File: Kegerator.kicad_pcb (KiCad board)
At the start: 2 copper layers, 200 x 21 mm, 17 parts, among them J1 Buttons, J2 LCD, J3 Temperature, J4 Programmer, J5 Control, U1 ESP32-S2-WROVER, U2 MCP1700

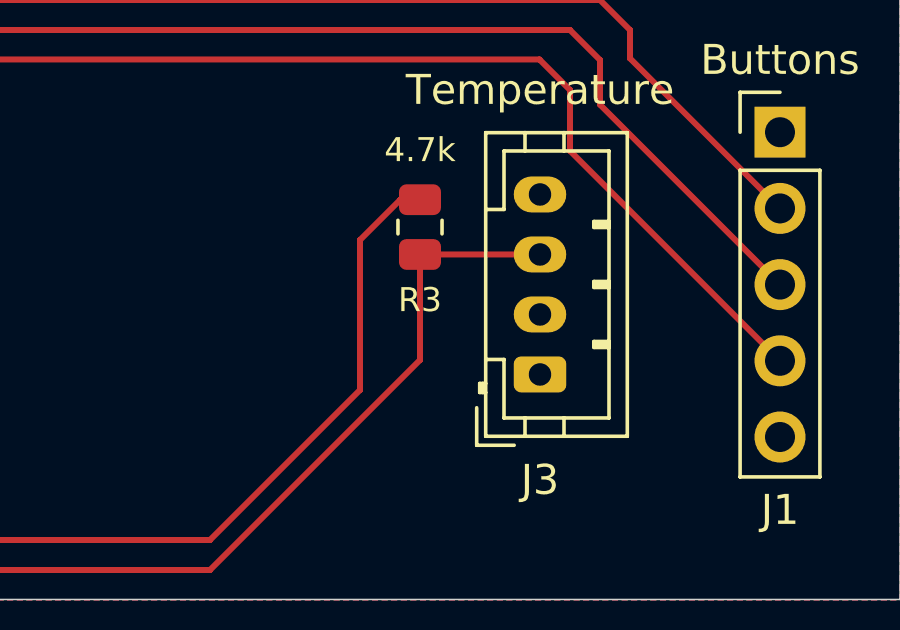
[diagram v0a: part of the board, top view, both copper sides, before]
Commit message: Allowing the temperature sensor to be able to be both really powered or parasitic power
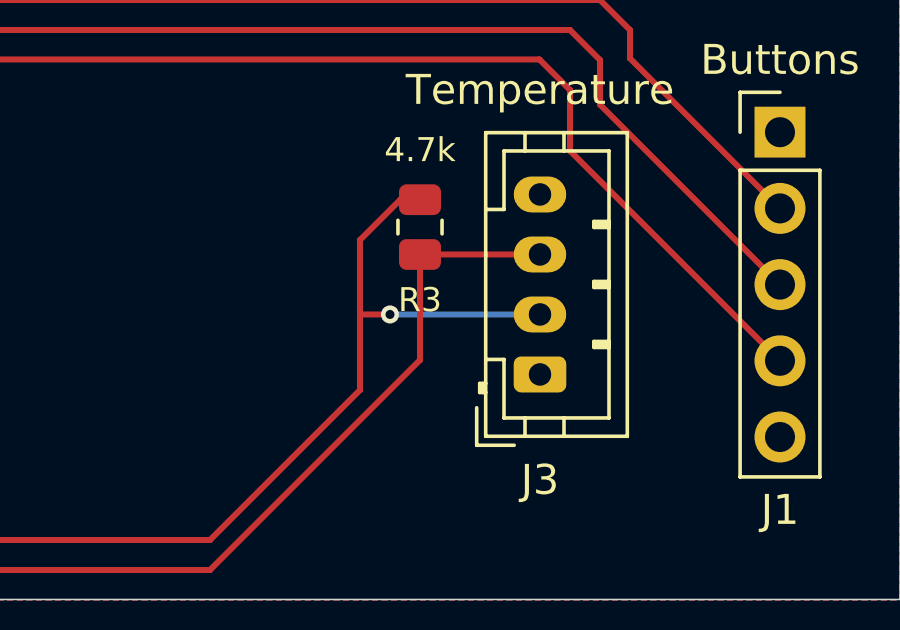
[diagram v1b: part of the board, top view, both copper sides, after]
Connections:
- J3 pad 2: unconnected-(J3-Pin_2-Pad2) -> +3V3
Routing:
- net +3V3: track 219.8 -> 225.8 mm, vias 2 -> 3
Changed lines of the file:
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@@
 	(net 37 "unconnected-(U1-IO08-Pad11)")
 	(net 38 "unconnected-(U1-IO37-Pad31)")
-	(net 39 "unconnected-(J3-Pin_2-Pad2)")
-	(net 40 "unconnected-(J3-Pin_1-Pad1)")
-	(net 41 "BOOT")
-	(net 42 "unconnected-(U1-IO14-Pad17)")
-	(net 43 "/HEAT")
-	(net 44 "HEATER")
-	(net 45 "/COOL")
-	(net 46 "unconnected-(J1-Pin_1-Pad1)")
+	(net 39 "unconnected-(J3-Pin_1-Pad1)")
+	(net 40 "BOOT")
+	(net 41 "unconnected-(U1-IO14-Pad17)")
+	(net 42 "/HEAT")
+	(net 43 "HEATER")
+	(net 44 "/COOL")
+	(net 45 "unconnected-(J1-Pin_1-Pad1)")
 	(footprint "Connector_JST:JST_XH_B4B-XH-A_1x04_P2.50mm_Vertical"
 		(layer "F.Cu")
@@
 			(layers "*.Cu" "*.Mask")
 			(remove_unused_layers no)
-			(net 45 "/COOL")
+			(net 44 "/COOL")
 			(pinfunction "Pin_3")
 			(pintype "passive")
@@
 			(layers "*.Cu" "*.Mask")
 			(remove_unused_layers no)
-			(net 43 "/HEAT")
+			(net 42 "/HEAT")
 			(pinfunction "Pin_4")
 			(pintype "passive")
@@
 			(layers "F.Cu" "F.Paste" "F.Mask")
 			(roundrect_rratio 0.243902)
-			(net 45 "/COOL")
+			(net 44 "/COOL")
 			(pintype "passive")
 		)
@@
 			(layers "*.Cu" "*.Mask")
 			(remove_unused_layers no)
-			(net 46 "unconnected-(J1-Pin_1-Pad1)")
+			(net 45 "unconnected-(J1-Pin_1-Pad1)")
 			(pinfunction "Pin_1")
 			(pintype "passive+no_connect")
@@
 			(layers "F.Cu" "F.Paste" "F.Mask")
 			(roundrect_rratio 0.243902)
-			(net 43 "/HEAT")
+			(net 42 "/HEAT")
 			(pintype "passive")
 		)
@@
 			(layers "F.Cu" "F.Paste" "F.Mask")
 			(roundrect_rratio 0.243902)
-			(net 44 "HEATER")
+			(net 43 "HEATER")
 			(pintype "passive")
 		)
@@
 			(size 1.5 0.9)
 			(layers "F.Cu" "F.Paste" "F.Mask")
-			(net 41 "BOOT")
+			(net 40 "BOOT")
 			(pinfunction "IO00")
 			(pintype "bidirectional")
@@
 			(size 0.9 1.5)
 			(layers "F.Cu" "F.Paste" "F.Mask")
-			(net 42 "unconnected-(U1-IO14-Pad17)")
+			(net 41 "unconnected-(U1-IO14-Pad17)")
 			(pinfunction "IO14")
 			(pintype "bidirectional+no_connect")
@@
 			(size 0.9 1.5)
 			(layers "F.Cu" "F.Paste" "F.Mask")
-			(net 44 "HEATER")
+			(net 43 "HEATER")
 			(pinfunction "IO18")
 			(pintype "bidirectional")
@@
 			(remove_unused_layers no)
 			(roundrect_rratio 0.208333)
-			(net 40 "unconnected-(J3-Pin_1-Pad1)")
+			(net 39 "unconnected-(J3-Pin_1-Pad1)")
 			(pinfunction "Pin_1")
-			(pintype "passive")
+			(pintype "passive+no_connect")
 		)
 		(pad "2" thru_hole oval
@@
 			(layers "*.Cu" "*.Mask")
 			(remove_unused_layers no)
-			(net 39 "unconnected-(J3-Pin_2-Pad2)")
+			(net 2 "+3V3")
 			(pinfunction "Pin_2")
 			(pintype "passive")
@@
 			(layers "*.Cu" "*.Mask")
 			(remove_unused_layers no)
-			(net 41 "BOOT")
+			(net 40 "BOOT")
 			(pinfunction "Pin_2")
 			(pintype "passive")
@@
 	)
 	(segment
+		(start 253.010389 37.482037)
+		(end 253 37.492426)
+		(width 0.2)
+		(layer "F.Cu")
+		(net 2)
+	)
+	(segment
 		(start 255 33.657037)
 		(end 254.342963 33.657037)
@@
 	)
 	(segment
+		(start 253 37.492426)
+		(end 253 37)
+		(width 0.2)
+		(layer "F.Cu")
+		(net 2)
+	)
+	(segment
 		(start 125.95 33.75)
 		(end 124.2 32)
@@
 	)
 	(segment
-		(start 253 40)
+		(start 253 37)
 		(end 253 35)
 		(width 0.2)
@@
 	)
 	(segment
+		(start 253 40)
+		(end 253 37.492426)
+		(width 0.2)
+		(layer "F.Cu")
+		(net 2)
+	)
+	(segment
 		(start 193.98 38.02)
 		(end 194 38)
@@
 	)
 	(segment
+		(start 254 37.482037)
+		(end 253.010389 37.482037)
+		(width 0.2)
+		(layer "F.Cu")
+		(net 2)
+	)
+	(segment
 		(start 81 43.5)
 		(end 81 45.107037)
@@
 	)
 	(via
+		(at 254 37.482037)
+		(size 0.6)
+		(drill 0.3)
+		(layers "F.Cu" "B.Cu")
+		(free yes)
+		(net 2)
+	)
+	(via
 		(at 121 32)
 		(size 0.6)
@@
 	)
 	(segment
+		(start 254 37.482037)
+		(end 259 37.482037)
+		(width 0.2)
+		(layer "B.Cu")
+		(net 2)
+	)
+	(segment
 		(start 83.99156 39.0875)
 		(end 81.07906 42)
@@
 		(width 0.2)
 		(layer "F.Cu")
-		(net 41)
+		(net 40)
 	)
 	(via
@@
 		(layers "F.Cu" "B.Cu")
 		(free yes)
-		(net 41)
+		(net 40)
 	)
 	(segment
@@
 		(width 0.2)
 		(layer "B.Cu")
-		(net 41)
+		(net 40)
 	)
 	(segment
@@
 		(width 0.2)
 		(layer "B.Cu")
-		(net 41)
+		(net 40)
 	)
 	(segment
@@
 		(width 0.2)
 		(layer "B.Cu")
-		(net 41)
+		(net 40)
 	)
 	(segment
@@
 		(width 0.2)
 		(layer "F.Cu")
-		(net 43)
+		(net 42)
 	)
 	(segment
@@
 		(width 0.2)
 		(layer "F.Cu")
-		(net 43)
+		(net 42)
 	)
 	(segment
@@
 		(width 0.2)
 		(layer "F.Cu")
-		(net 44)
+		(net 43)
 	)
 	(segment
@@
 		(width 0.2)
 		(layer "F.Cu")
-		(net 44)
+		(net 43)
 	)
 	(segment
@@
 		(width 0.2)
 		(layer "F.Cu")
-		(net 45)
+		(net 44)
 	)
 	(zone

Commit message: Few cleanups
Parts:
- moved J3 3.00 mm to (256.0, 39.5)
- moved R3 3.00 mm to (252.0, 34.6)
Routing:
- net TEMP: track 164.8 -> 161.8 mm
- net +3V3: track 225.8 -> 222.8 mm
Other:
- board text added: "+5V"
- board text added: "COOL"
- board text added: "DOWN"
- board text added: "HEAT"
- board text added: "Kegerator temperature controller"
- board text added: "UNITS"
- board text added: "UP"
- board text added: "https://github.com/madpilot/kegerator"
- board text added: "v1.0.0"
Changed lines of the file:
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@@
 	(net 45 "unconnected-(J1-Pin_1-Pad1)")
 	(footprint "Connector_JST:JST_XH_B4B-XH-A_1x04_P2.50mm_Vertical"
+		(locked yes)
 		(layer "F.Cu")
 		(at 115 32.75 -90)
@@
 	(footprint "Resistor_SMD:R_0805_2012Metric"
 		(layer "F.Cu")
-		(at 255 34.569537 -90)
+		(at 252 34.569537 -90)
 		(descr "Resistor SMD 0805 (2012 Metric), square (rectangular) end terminal, IPC_7351 nominal, (Body size source: IPC-SM-782 page 72, https://www.pcb-3d.com/wordpress/wp-content/uploads/ipc-sm-782a_amendment_1_and_2.pdf), generated with kicad-footprint-generator")
 		(tags "resistor")
@@
 	(footprint "Connector_JST:JST_PH_B4B-PH-K_1x04_P2.00mm_Vertical"
 		(layer "F.Cu")
-		(at 259 39.482037 90)
+		(at 256 39.482037 90)
 		(descr "JST PH series connector, B4B-PH-K (http://www.jst-mfg.com/product/pdf/eng/ePH.pdf), generated with kicad-footprint-generator")
 		(tags "connector JST PH side entry")
@@
 		(layer "Edge.Cuts")
 	)
+	(gr_text "HEAT\n"
+		(at 113.49598 40.831 -0)
+		(layer "B.SilkS")
+		(effects
+			(font
+				(size 0.8 0.8)
+				(thickness 0.2)
+				(bold yes)
+			)
+			(justify left bottom mirror)
+		)
+	)
+	(gr_text "GND"
+		(at 113.49598 33.331 0)
+		(layer "B.SilkS")
+		(effects
+			(font
+				(size 0.8 0.8)
+				(thickness 0.2)
+				(bold yes)
+			)
+			(justify left bottom mirror)
+		)
+	)
+	(gr_text "+5V"
+		(at 113.49598 35.831 -0)
+		(layer "B.SilkS")
+		(effects
+			(font
+				(size 0.8 0.8)
+				(thickness 0.2)
+				(bold yes)
+			)
+			(justify left bottom mirror)
+		)
+	)
+	(gr_text "COOL"
+		(at 113.49598 38.331 -0)
+		(layer "B.SilkS")
+		(effects
+			(font
+				(size 0.8 0.8)
+				(thickness 0.2)
+				(bold yes)
+			)
+			(justify left bottom mirror)
+		)
+	)
+	(gr_text "Kegerator temperature controller"
+		(at 209.46605 36 0)
+		(layer "F.SilkS")
+		(effects
+			(font
+				(size 1.5 1.5)
+				(thickness 0.3)
+				(bold yes)
+			)
+			(justify left bottom)
+		)
+	)
 	(gr_text "3.3V"
 		(at 134 30.676725 0)
@@
 		)
 	)
+	(gr_text "\nUP"
+		(at 263.307249 34.479115 0)
+		(layer "F.SilkS")
+		(effects
+			(font
+				(size 0.8 0.8)
+				(thickness 0.2)
+				(bold yes)
+			)
+			(justify left bottom)
+		)
+	)
 	(gr_text "GND"
 		(at 134 43.376725 0)
@@
 		)
 	)
+	(gr_text "v1.0.0"
+		(at 258 46 0)
+		(layer "F.SilkS")
+		(effects
+			(font
+				(size 1.5 1.5)
+				(thickness 0.3)
+				(bold yes)
+			)
+			(justify left bottom)
+		)
+	)
+	(gr_text "DOWN\n"
+		(at 261.554064 36.92542 0)
+		(layer "F.SilkS")
+		(effects
+			(font
+				(size 0.8 0.8)
+				(thickness 0.2)
+				(bold yes)
+			)
+			(justify left bottom)
+		)
+	)
 	(gr_text "EN"
 		(at 134 38.296725 0)
@@
 		)
 	)
+	(gr_text "GND"
+		(at 262.451042 41.981115 0)
+		(layer "F.SilkS")
+		(effects
+			(font
+				(size 0.8 0.8)
+				(thickness 0.2)
+				(bold yes)
+			)
+			(justify left bottom)
+		)
+	)
+	(gr_text "https://github.com/madpilot/kegerator"
+		(at 209.732791 38 0)
+		(layer "F.SilkS")
+		(effects
+			(font
+				(size 1 1)
+				(thickness 0.25)
+				(bold yes)
+			)
+			(justify left bottom)
+		)
+	)
+	(gr_text "UNITS\n"
+		(at 261.460566 39.441115 0)
+		(layer "F.SilkS")
+		(effects
+			(font
+				(size 0.8 0.8)
+				(thickness 0.2)
+				(bold yes)
+			)
+			(justify left bottom)
+		)
+	)
 	(dimension
 		(type aligned)
@@
 	)
 	(segment
-		(start 253.010389 37.482037)
-		(end 253 37.492426)
+		(start 250.010389 37.482037)
+		(end 250 37.492426)
 		(width 0.2)
 		(layer "F.Cu")
@@
 	)
 	(segment
-		(start 255 33.657037)
-		(end 254.342963 33.657037)
+		(start 252 33.657037)
+		(end 251.342963 33.657037)
 		(width 0.2)
 		(layer "F.Cu")
@@
 	)
 	(segment
-		(start 253 37.492426)
-		(end 253 37)
+		(start 250 37.492426)
+		(end 250 37)
 		(width 0.2)
 		(layer "F.Cu")
@@
 	)
 	(segment
-		(start 201 45)
-		(end 248 45)
-		(width 0.2)
-		(layer "F.Cu")
-		(net 2)
-	)
-	(segment
-		(start 253 37)
-		(end 253 35)
+		(start 250 37)
+		(end 250 35)
 		(width 0.2)
 		(layer "F.Cu")
@@
 	)
 	(segment
-		(start 253 40)
-		(end 253 37.492426)
+		(start 250 40)
+		(end 250 37.492426)
 		(width 0.2)
 		(layer "F.Cu")
@@
 	)
 	(segment
-		(start 248 45)
-		(end 253 40)
+		(start 250 40)
+		(end 245 45)
 		(width 0.2)
 		(layer "F.Cu")
@@
 	)
 	(segment
-		(start 254.342963 33.657037)
-		(end 253 35)
+		(start 201 45)
+		(end 245 45)
+		(width 0.2)
+		(layer "F.Cu")
+		(net 2)
+	)
+	(segment
+		(start 251.342963 33.657037)
+		(end 250 35)
 		(width 0.2)
 		(layer "F.Cu")
@@
 	)
 	(segment
-		(start 254 37.482037)
-		(end 253.010389 37.482037)
+		(start 251 37.482037)
+		(end 250.010389 37.482037)
 		(width 0.2)
 		(layer "F.Cu")
@@
 	)
 	(via
-		(at 254 37.482037)
+		(at 251 37.482037)
 		(size 0.6)
 		(drill 0.3)
@@
 	)
 	(segment
-		(start 254 37.482037)
-		(end 259 37.482037)
+		(start 251 37.482037)
+		(end 256 37.482037)
 		(width 0.2)
 		(layer "B.Cu")
@@
 	)
 	(segment
-		(start 248 46)
-		(end 255 39)
+		(start 103.732037 41.732037)
+		(end 108 46)
 		(width 0.2)
 		(layer "F.Cu")
@@
 	)
 	(segment
-		(start 103.732037 41.732037)
-		(end 108 46)
+		(start 252 39)
+		(end 245 46)
 		(width 0.2)
 		(layer "F.Cu")
@@
 	(segment
 		(start 108 46)
-		(end 248 46)
+		(end 245 46)
 		(width 0.2)
 		(layer "F.Cu")
@@
 	)
 	(segment
-		(start 255 39)
-		(end 255 35.482037)
+		(start 256 35.482037)
+		(end 252 35.482037)
 		(width 0.2)
 		(layer "F.Cu")
@@
 	)
 	(segment
-		(start 259 35.482037)
-		(end 255 35.482037)
+		(start 252 35.482037)
+		(end 252 39)
 		(width 0.2)
 		(layer "F.Cu")

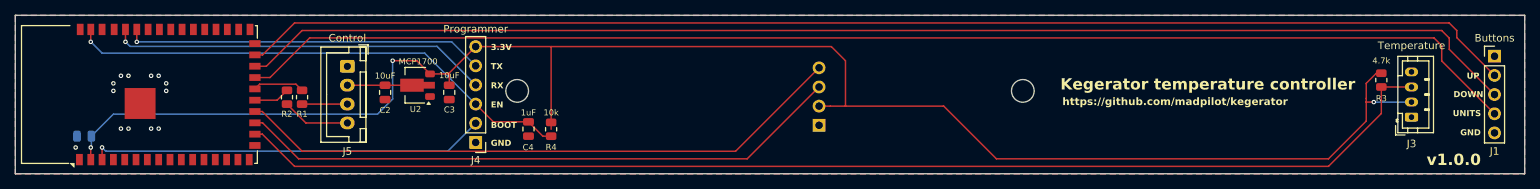
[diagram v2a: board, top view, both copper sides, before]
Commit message: Adjusting LCD and screw positions
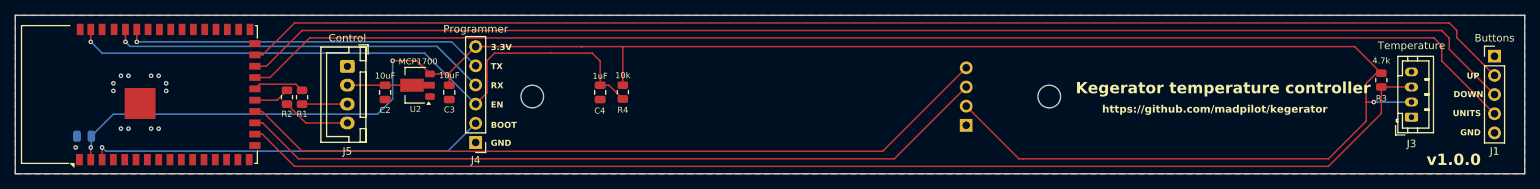
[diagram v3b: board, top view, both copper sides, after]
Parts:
- moved J2 19.5 mm to (180.0, 36.8)
- moved R4 10.7 mm to (151.5, 36.2)
- moved C4 10.7 mm to (148.5, 36.2)
- moved H2 3.58 mm to (208.0, 36.8)
- moved H1 2.14 mm to (139.5, 36.8)
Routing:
- net +3V3: track 222.8 -> 263.2 mm
- net SDA: track 81.8 -> 101.3 mm
- net SCL: track 81.3 -> 100.8 mm
- net EN: track 67.9 -> 74.4 mm
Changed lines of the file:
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@@
 	(footprint "Resistor_SMD:R_0805_2012Metric"
 		(layer "F.Cu")
-		(at 142 41.0875 -90)
+		(at 151.5 36.1625 -90)
 		(descr "Resistor SMD 0805 (2012 Metric), square (rectangular) end terminal, IPC_7351 nominal, (Body size source: IPC-SM-782 page 72, https://www.pcb-3d.com/wordpress/wp-content/uploads/ipc-sm-782a_amendment_1_and_2.pdf), generated with kicad-footprint-generator")
 		(tags "resistor")
@@
 	(footprint "MountingHole:MountingHole_3mm"
 		(layer "F.Cu")
-		(at 204.5 36)
+		(at 208 36.75)
 		(descr "Mounting Hole 3mm, no annular")
 		(tags "mounting hole 3mm no annular")
@@
 	)
 	(footprint "Capacitor_SMD:C_0805_2012Metric"
+		(locked yes)
 		(layer "F.Cu")
 		(at 128.5 36.2 -90)
@@
 	(footprint "Capacitor_SMD:C_0805_2012Metric"
 		(layer "F.Cu")
-		(at 139 41.05 -90)
+		(at 148.5 36.2 -90)
 		(descr "Capacitor SMD 0805 (2012 Metric), square (rectangular) end terminal, IPC_7351 nominal, (Body size source: IPC-SM-782 page 76, https://www.pcb-3d.com/wordpress/wp-content/uploads/ipc-sm-782a_amendment_1_and_2.pdf, https://docs.google.com/spreadsheets/d/1BsfQQcO9C6DZCsRaXUlFlo91Tg2WpOkGARC1WS5S8t0/edit?usp=sharing), generated with kicad-footprint-generator")
 		(tags "capacitor")
@@
 	(footprint "MountingHole:MountingHole_3mm"
 		(layer "F.Cu")
-		(at 137.5 36)
+		(at 139.5 36.75)
 		(descr "Mounting Hole 3mm, no annular")
 		(tags "mounting hole 3mm no annular")
@@
 	(footprint "Display:0.91 Inch OLED Module 128X32"
 		(layer "B.Cu")
-		(at 160.5 36.75)
+		(at 180 36.75)
 		(property "Reference" "J2"
 			(at 0 0.5 -90)
@@
 		)
 	)
+	(gr_line
+		(start 133.5 32)
+		(end 133.5 34)
+		(stroke
+			(width 0.2)
+			(type default)
+		)
+		(layer "F.Cu")
+		(net 5)
+	)
+	(gr_line
+		(start 134.5 31)
+		(end 133.5 32)
+		(stroke
+			(width 0.2)
+			(type default)
+		)
+		(layer "F.Cu")
+		(net 5)
+	)
+	(gr_line
+		(start 142 31)
+		(end 134.5 31)
+		(stroke
+			(width 0.2)
+			(type default)
+		)
+		(layer "F.Cu")
+		(net 5)
+	)
 	(gr_rect
 		(start 71 25.982037)
@@
 	)
 	(gr_text "Kegerator temperature controller"
-		(at 209.46605 36 0)
+		(at 211.5 36.5 0)
 		(layer "F.SilkS")
 		(effects
@@
 	)
 	(gr_text "https://github.com/madpilot/kegerator"
-		(at 209.732791 38 0)
+		(at 215 39 0)
 		(layer "F.SilkS")
 		(effects
@@
 	)
 	(segment
-		(start 194 38)
-		(end 201 45)
+		(start 151.5 35.25)
+		(end 151.5 30.132037)
 		(width 0.2)
 		(layer "F.Cu")
@@
 	)
 	(segment
+		(start 197 38.02)
+		(end 203.98 45)
+		(width 0.2)
+		(layer "F.Cu")
+		(net 2)
+	)
+	(segment
 		(start 250 37.492426)
 		(end 250 37)
@@
 	)
 	(segment
-		(start 181 32)
-		(end 181 38.02)
+		(start 142 30.132037)
+		(end 146 30.132037)
 		(width 0.2)
 		(layer "F.Cu")
@@
 	)
 	(segment
-		(start 142 39)
-		(end 142 41.0875)
+		(start 245 45)
+		(end 204.5 45)
 		(width 0.2)
 		(layer "F.Cu")
@@
 	)
 	(segment
-		(start 125.95 33.75)
-		(end 128.382037 33.75)
+		(start 203.98 45)
+		(end 204.5 45)
 		(width 0.2)
 		(layer "F.Cu")
@@
 	)
 	(segment
-		(start 250 40)
-		(end 250 37.492426)
+		(start 151.5 30.132037)
+		(end 248.475 30.132037)
 		(width 0.2)
 		(layer "F.Cu")
@@
 	)
 	(segment
-		(start 193.98 38.02)
-		(end 194 38)
+		(start 125.95 33.75)
+		(end 128.382037 33.75)
 		(width 0.2)
 		(layer "F.Cu")
@@
 	(segment
 		(start 250 40)
-		(end 245 45)
+		(end 250 37.492426)
 		(width 0.2)
 		(layer "F.Cu")
@@
 	)
 	(segment
-		(start 201 45)
+		(start 250 40)
 		(end 245 45)
 		(width 0.2)
@@
 	)
 	(segment
-		(start 81 43.5)
-		(end 81 45.107037)
-		(width 0.2)
-		(layer "F.Cu")
-		(net 2)
-	)
-	(segment
-		(start 177.5 38.02)
-		(end 179 38.02)
+		(start 248.475 30.132037)
+		(end 252 33.657037)
 		(width 0.2)
 		(layer "F.Cu")
@@
 	)
 	(segment
-		(start 128.5 33.632037)
-		(end 128.5 35.25)
-		(width 0.2)
-		(layer "F.Cu")
-		(net 2)
-	)
-	(segment
-		(start 179 38.02)
-		(end 181 38.02)
-		(width 0.2)
-		(layer "F.Cu")
-		(net 2)
-	)
-	(segment
-		(start 179.132037 30.132037)
-		(end 181 32)
+		(start 81 43.5)
+		(end 81 45.107037)
 		(width 0.2)
 		(layer "F.Cu")
@@
 	)
 	(segment
-		(start 142 30.132037)
-		(end 142 39)
+		(start 146 30.132037)
+		(end 151.5 30.132037)
 		(width 0.2)
 		(layer "F.Cu")
@@
 	)
 	(segment
-		(start 181 38.02)
-		(end 193.98 38.02)
+		(start 128.5 33.632037)
+		(end 128.5 35.25)
 		(width 0.2)
 		(layer "F.Cu")
@@
 	)
 	(segment
-		(start 142 30.132037)
-		(end 179.132037 30.132037)
+		(start 146.05 30.182037)
+		(end 146 30.132037)
 		(width 0.2)
 		(layer "F.Cu")
@@
 	)
 	(segment
+		(start 147.45 31)
+		(end 148.5 32.05)
+		(width 0.2)
+		(layer "F.Cu")
+		(net 5)
+	)
+	(segment
 		(start 81 29.5)
 		(end 81 27.857037)
@@
 	)
 	(segment
-		(start 142 42)
-		(end 140.9 42)
+		(start 148.5 32.05)
+		(end 148.5 35.25)
+		(width 0.2)
+		(layer "F.Cu")
+		(net 5)
+	)
+	(segment
+		(start 148.5 35.625)
+		(end 148.5 35.5375)
 		(width 0.2)
 		(layer "F.Cu")
@@
 	)
 	(segment
-		(start 134.347963 40.1)
-		(end 132 37.752037)
+		(start 132 37.752037)
+		(end 133.5 36.252037)
 		(width 0.2)
 		(layer "F.Cu")
@@
 	)
 	(segment
-		(start 140.9 42)
-		(end 139 40.1)
+		(start 149.675 35.25)
+		(end 151.5 37.075)
 		(width 0.2)
 		(layer "F.Cu")
@@
 	)
 	(segment
-		(start 139 40.175)
-		(end 139 40.0875)
+		(start 148.5 35.25)
+		(end 149.675 35.25)
 		(width 0.2)
 		(layer "F.Cu")
@@
 	)
 	(segment
-		(start 139 40.1)
-		(end 134.347963 40.1)
+		(start 133.5 36.252037)
+		(end 133.5 34)
+		(width 0.2)
+		(layer "F.Cu")
+		(net 5)
+	)
+	(segment
+		(start 142 31)
+		(end 147.45 31)
 		(width 0.2)
 		(layer "F.Cu")
@@
 	)
 	(segment
-		(start 167.98 45)
-		(end 108.535926 45)
+		(start 102.42906 40.232037)
+		(end 102.661097 40)
 		(width 0.2)
 		(layer "F.Cu")
@@
 	)
 	(segment
-		(start 103.767963 40.232037)
-		(end 102.42906 40.232037)
+		(start 197 35.48)
+		(end 187.48 45)
 		(width 0.2)
 		(layer "F.Cu")
@@
 	)
 	(segment
-		(start 102.661097 40)
+		(start 103.767963 40.232037)
 		(end 102.42906 40.232037)
 		(width 0.2)
@@
 	)
 	(segment
-		(start 177.5 35.48)
-		(end 167.98 45)
+		(start 187.48 45)
+		(end 108.535926 45)
 		(width 0.2)
 		(layer "F.Cu")
@@
 	)
 	(segment
-		(start 109 44)
-		(end 103.732037 38.732037)
+		(start 103.732037 38.732037)
+		(end 102.42906 38.732037)
 		(width 0.2)
 		(layer "F.Cu")
@@
 	)
 	(segment
-		(start 166.44 44)
-		(end 109 44)
+		(start 109 44)
+		(end 103.732037 38.732037)
 		(width 0.2)
 		(layer "F.Cu")
@@
 	)
 	(segment
-		(start 177.5 32.94)
-		(end 166.44 44)
+		(start 185.94 44)
+		(end 109 44)
 		(width 0.2)
 		(layer "F.Cu")
@@
 	)
 	(segment
-		(start 103.732037 38.732037)
-		(end 102.42906 38.732037)
+		(start 197 32.94)
+		(end 185.94 44)
 		(width 0.2)
 		(layer "F.Cu")

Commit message: Final adjustments to screw layouts and cleaning up some tracks
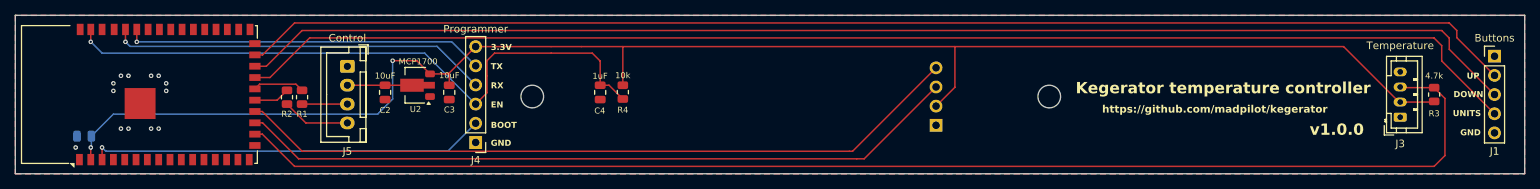
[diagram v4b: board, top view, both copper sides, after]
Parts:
- moved R3 7.26 mm to (259.0, 36.5), turned to 90 degrees
- moved J2 4.00 mm to (176.0, 36.8)
- moved J3 1.50 mm to (254.5, 39.5)
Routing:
- net TEMP: track 161.8 -> 23.5 mm
- net +3V3: track 263.2 -> 209.1 mm, vias 3 -> 2
- net SDA: track 101.3 -> 97.3 mm
- net SCL: track 100.8 -> 96.8 mm
